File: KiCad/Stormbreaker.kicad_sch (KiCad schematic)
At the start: 46 parts, among them J1 Micro_SD_Card_Det2, J2 USB_C_Receptacle_USB2.0_14P, J3 Conn_01x03, J4 FAN, J5 Conn_01x02, Q1 PMOS, Q2 NMOS, SW1 SW_Push, U1 BQ25895RTW, U3 ATtiny1616-M

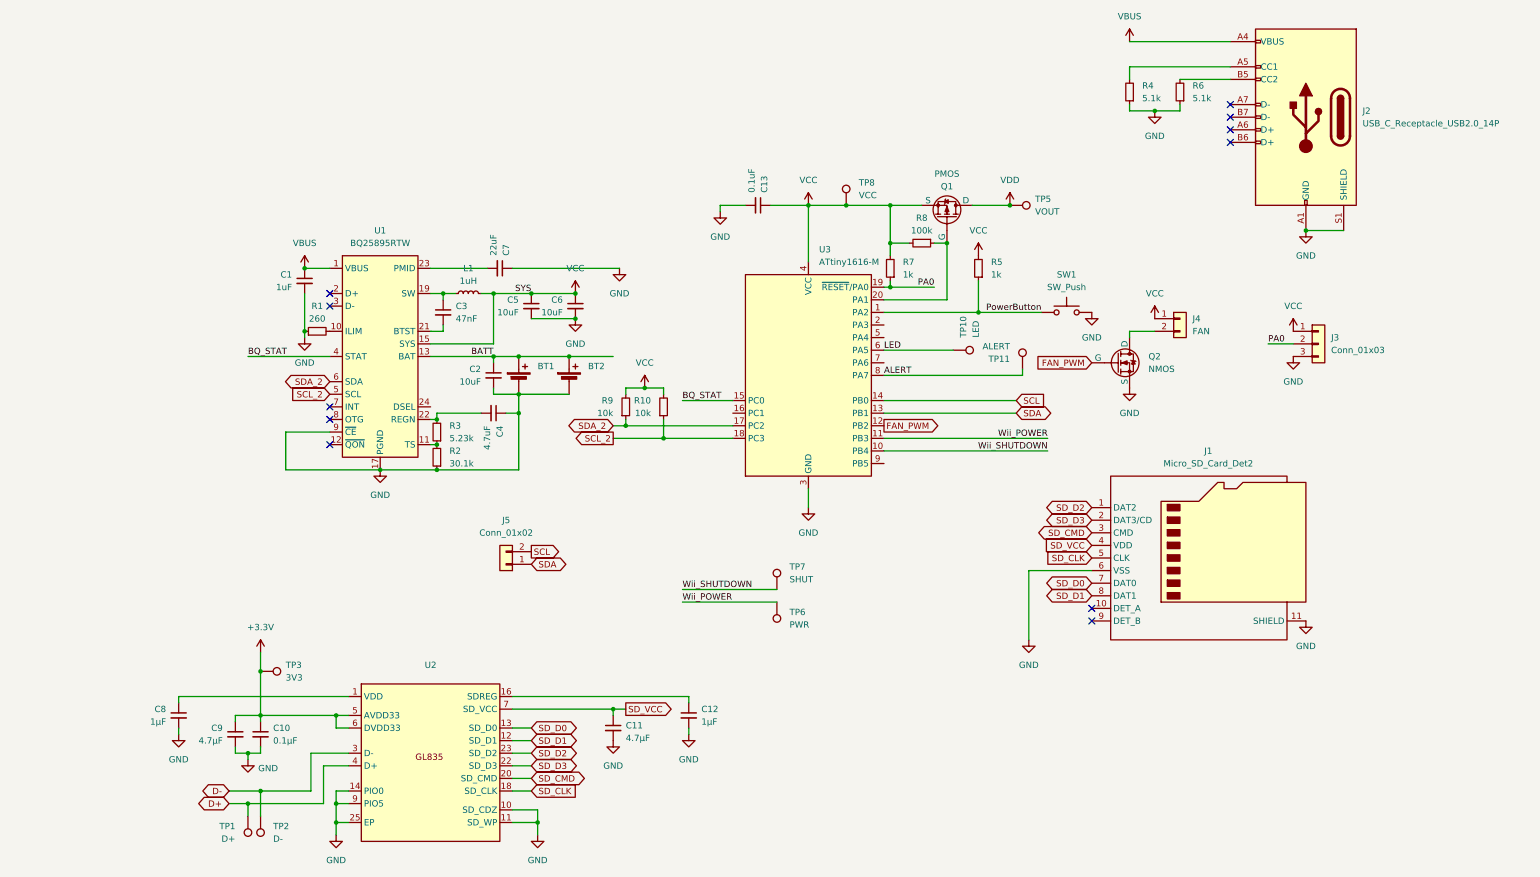
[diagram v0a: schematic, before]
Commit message: Add USB-C PD circuitry
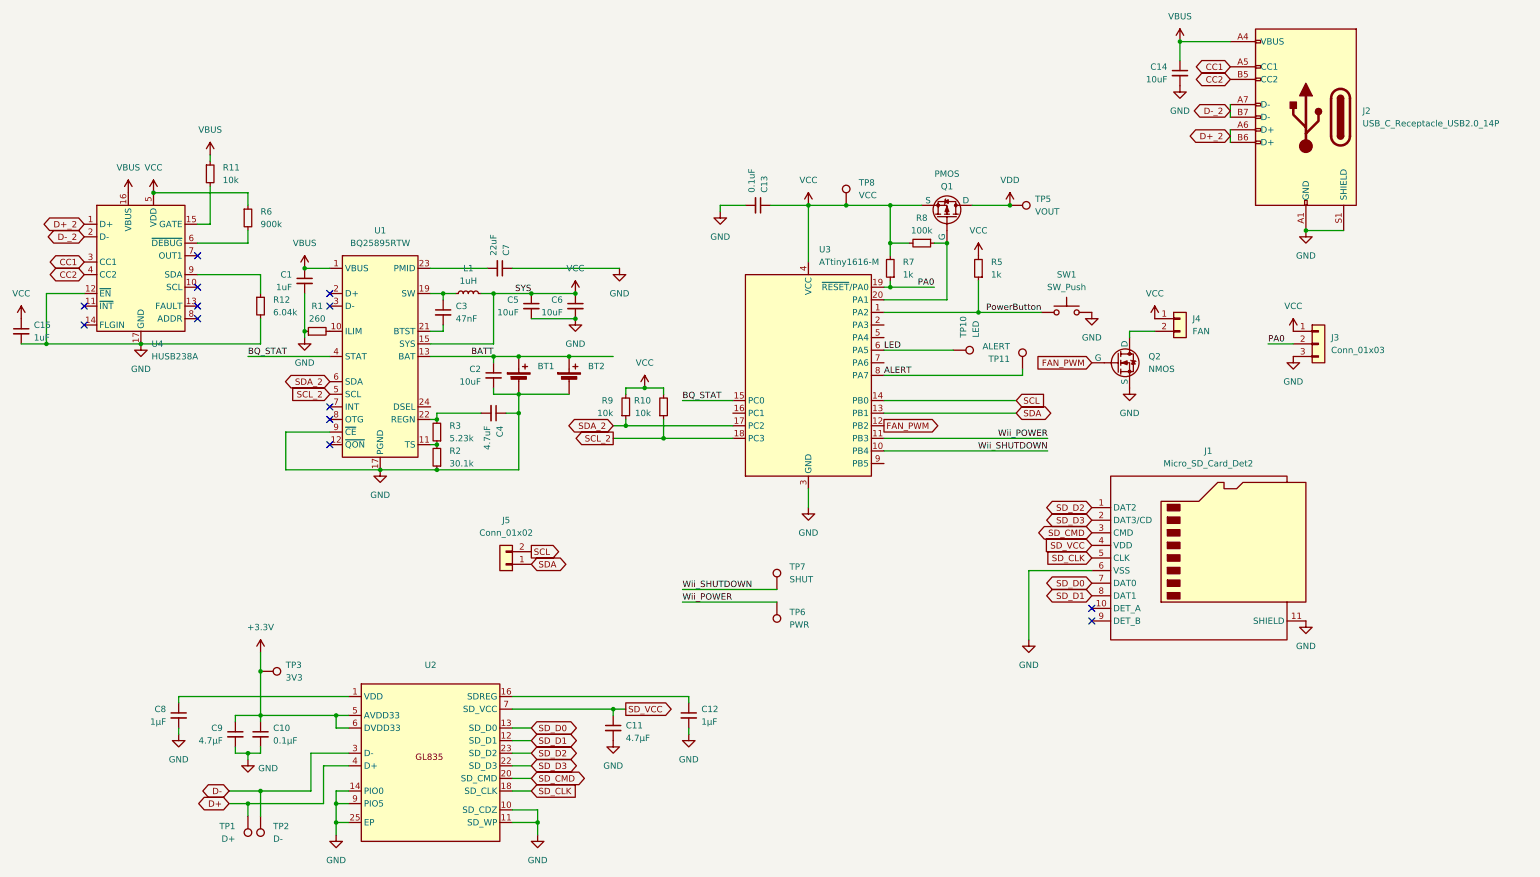
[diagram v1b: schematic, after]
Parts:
- removed R4: 5.1k, Resistor_SMD:R_0603_1608Metric, symbol Device:R_Small
- added C14: 10uF, Capacitor_SMD:C_0603_1608Metric, symbol Device:C_Small
- added C15: 1uF, Capacitor_SMD:C_0402_1005Metric, symbol Device:C_Small
- added R11: 10k, Resistor_SMD:R_0402_1005Metric, symbol Device:R_Small
- added R12: 6.04k, Resistor_SMD:R_0402_1005Metric, symbol Device:R_Small
- added U4: HUSB238A, Package_DFN_QFN:QFN-16-1EP_3x3mm_P0.5mm_EP1.7x1.7mm_ThermalVias, symbol Stormbreaker:HUSB238A
- R6: value 5.1k -> 900k; footprint Resistor_SMD:R_0603_1608Metric -> Resistor_SMD:R_0402_1005Metric
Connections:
- net GND: now also C14.2, C15.2, R12.2, U4.12 (~{EN}), U4.17 (GND); no longer R6.1
- net VBUS: now also C14.1, R11.1, U4.16 (VBUS)
- net VCC: now also R6.1, C15.1, U4.5 (VDD)
- net at R6.2: now also U4.6 (~{DEBUG}); no longer J2.B5 (CC2)
- net CC1: now reaches J2.A5 (CC1)
- net CC1: now also U4.3 (CC1)
- net D+_2: now reaches J2.A6 (D+)
- net D+_2: now also J2.B6 (D+), U4.1 (D+)
- net D-_2: now reaches J2.A7 (D-)
- net D-_2: now also J2.B7 (D-), U4.2 (D-)
- new net: R11.2, U4.15 (GATE)
- new net: R12.1, U4.9 (SDA)
- new net CC2: J2.B5 (CC2), U4.4 (CC2)
- no-connect marks 11 -> 13

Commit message: Adjustments to PD chip, WIP
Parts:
- C15: value 1uF -> 1μF
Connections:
- net VBUS: now also R6.1
- net VCC: no longer C15.1, R6.1, U4.5 (VDD)
- removed net D+_2: J2.A6 (D+), J2.B6 (D+), U4.1 (D+)
- removed net D-_2: J2.A7 (D-), J2.B7 (D-), U4.2 (D-)
- new net: C15.1, U4.5 (VDD)
- no-connect marks 13 -> 19

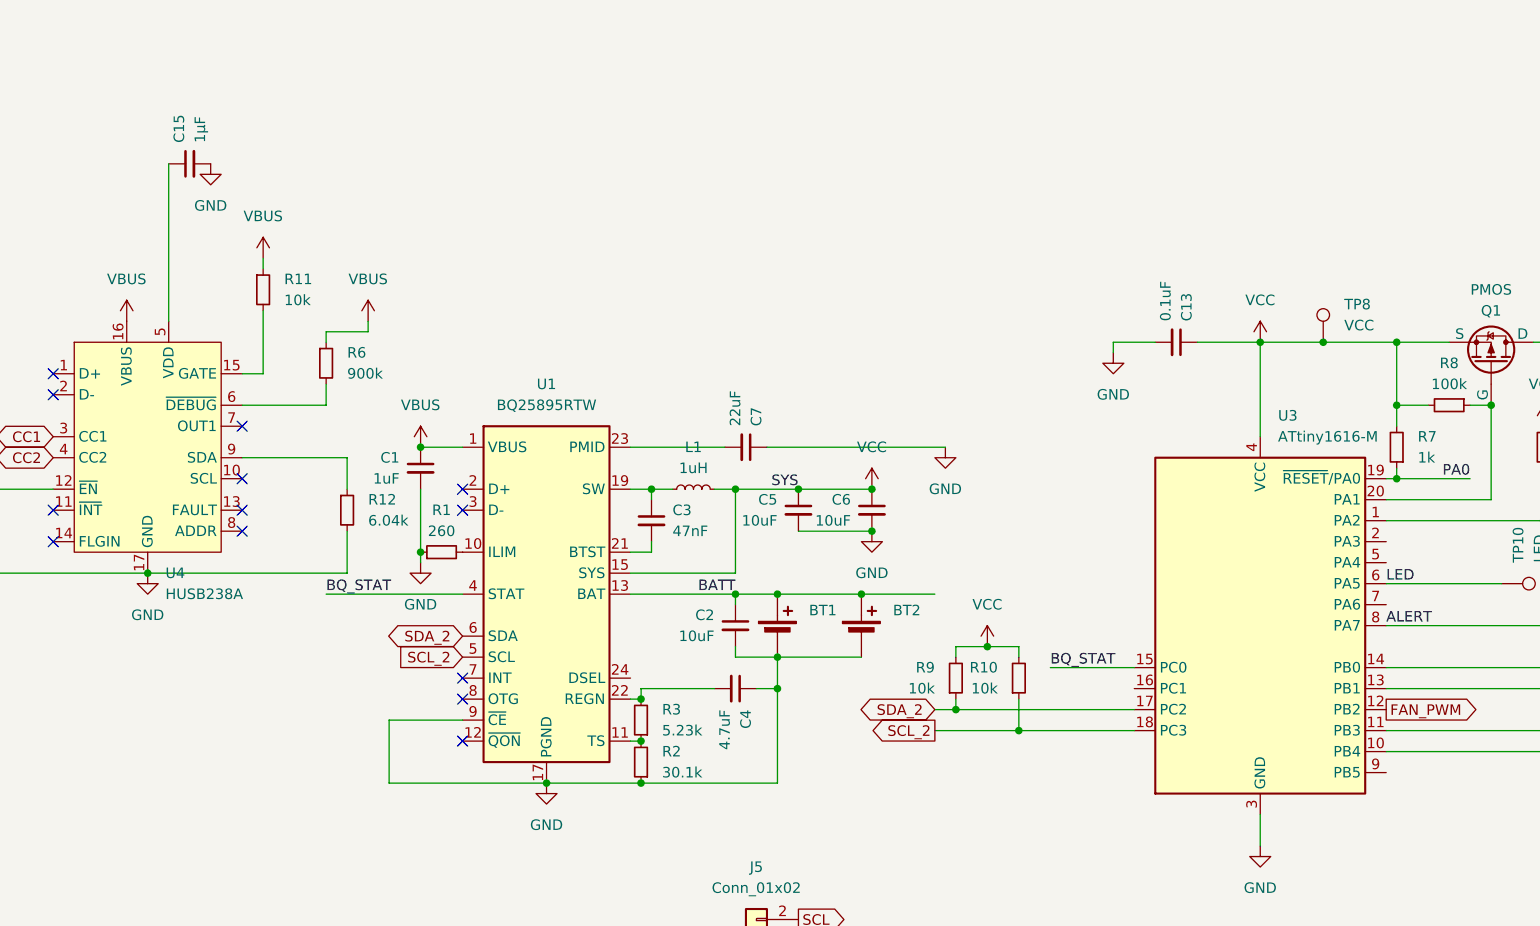
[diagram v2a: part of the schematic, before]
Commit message: Teardropped pads, slight footprint adjustments
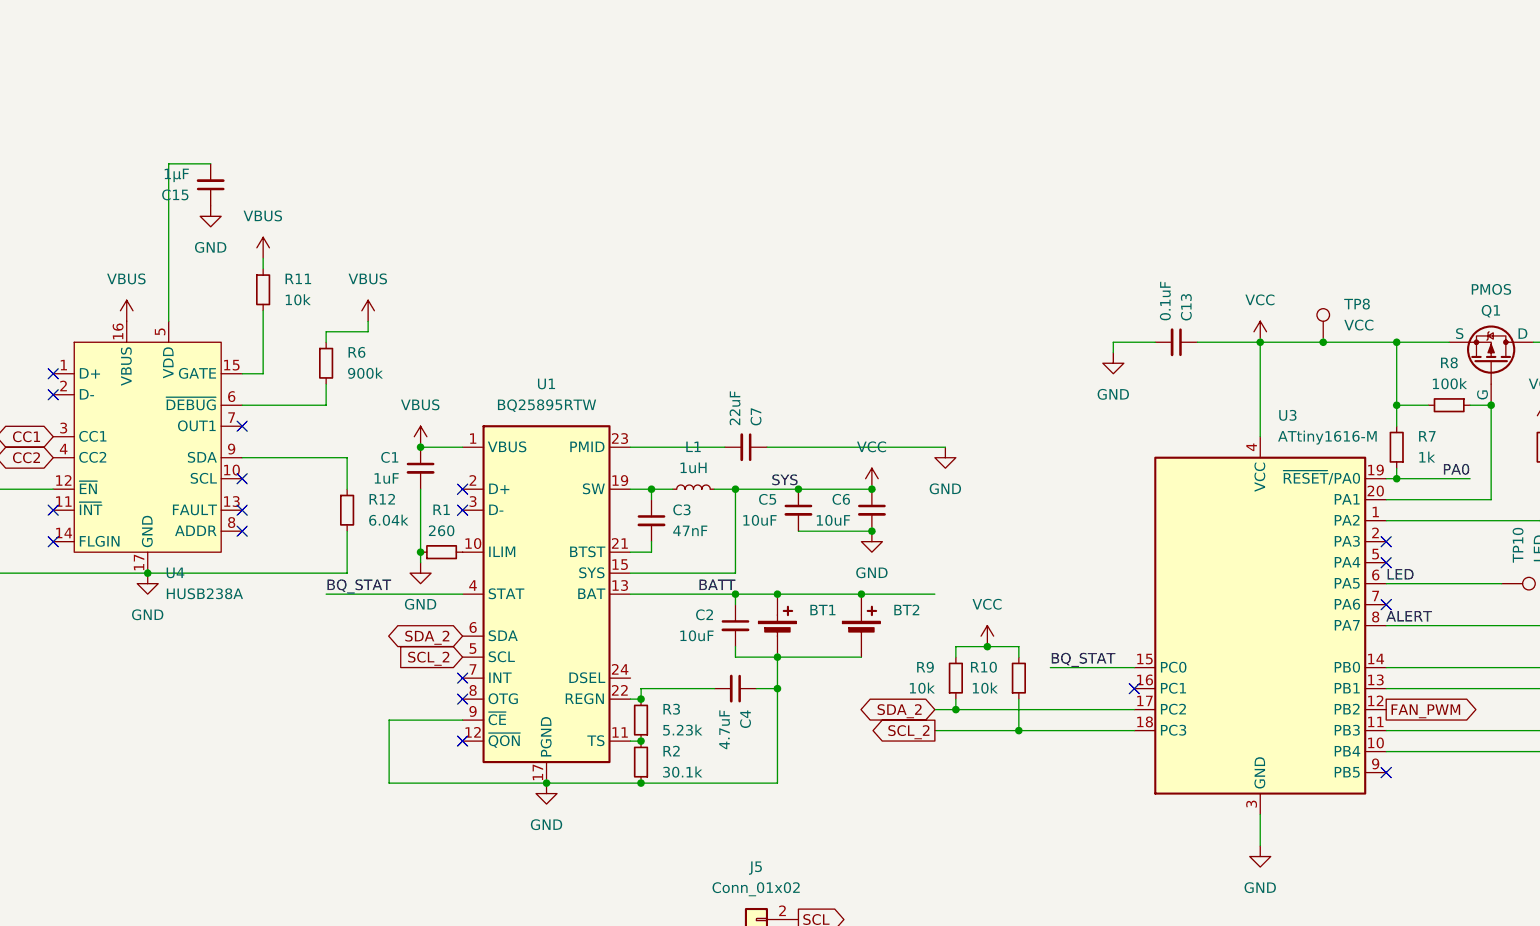
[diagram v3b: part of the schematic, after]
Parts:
- C15: footprint Capacitor_SMD:C_0402_1005Metric -> Capacitor_SMD:C_0603_1608Metric
- TP1, TP2, TP6, TP7: footprint TestPoint:TestPoint_Pad_D1.0mm -> Stormbreaker:TestPoint_Pad_D1.0mm_Small
- TP10, TP11: footprint TestPoint:TestPoint_Pad_D1.0mm -> Stormbreaker:TestPoint_Pad_D0.75mm_Small
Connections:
- net GND: now also C15.1; no longer C15.2
- net at U4.5 (VDD): now also C15.2; no longer C15.1
- no-connect marks 19 -> 24
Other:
- moved on the sheet: C15
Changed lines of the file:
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@@
 	)
 	(no_connect
+		(at 187.96 77.47)
+	)
+	(no_connect
 		(at 257.81 33.02)
 	)
 	(no_connect
+		(at 157.48 95.25)
+	)
+	(no_connect
 		(at 76.2 73.66)
 	)
@@
 	)
 	(no_connect
+		(at 187.96 105.41)
+	)
+	(no_connect
 		(at 229.87 134.62)
 	)
@@
 	)
 	(no_connect
+		(at 187.96 85.09)
+	)
+	(no_connect
+		(at 187.96 80.01)
+	)
+	(no_connect
 		(at 49.53 63.5)
 	)
@@
 	(wire
 		(pts
+			(xy 40.64 31.75) (xy 45.72 31.75)
+		)
+		(stroke
+			(width 0)
+			(type default)
+		)
+	)
+	(wire
+		(pts
 			(xy 147.32 92.71) (xy 157.48 92.71)
 		)
@@
 			)
 		)
-		(property "Footprint" "TestPoint:TestPoint_Pad_D1.0mm"
+		(property "Footprint" "Stormbreaker:TestPoint_Pad_D0.75mm_Small"
 			(at 201.93 87.63 0)
 			(effects
@@
 		(lib_name "GND_1")
 		(lib_id "power:GND")
-		(at 45.72 31.75 0)
+		(at 45.72 36.83 0)
 		(unit 1)
 		(exclude_from_sim no)
@@
 		(fields_autoplaced yes)
 		(property "Reference" "#PWR034"
-			(at 45.72 38.1 0)
+			(at 45.72 43.18 0)
 			(effects
 				(font
@@
 		)
 		(property "Value" "GND"
-			(at 45.72 36.83 0)
+			(at 45.72 41.91 0)
 			(effects
 				(font
@@
 		)
 		(property "Footprint" ""
-			(at 45.72 31.75 0)
+			(at 45.72 36.83 0)
 			(effects
 				(font
@@
 		)
 		(property "Datasheet" ""
-			(at 45.72 31.75 0)
+			(at 45.72 36.83 0)
 			(effects
 				(font
@@
 		)
 		(property "Description" "Power symbol creates a global label with name \"GND\" , ground"
-			(at 45.72 31.75 0)
+			(at 45.72 36.83 0)
 			(effects
 				(font
@@
 			)
 		)
-		(property "Footprint" "TestPoint:TestPoint_Pad_D1.0mm"
+		(property "Footprint" "Stormbreaker:TestPoint_Pad_D1.0mm_Small"
 			(at 171.45 130.81 0)
 			(effects
@@
 			)
 		)
-		(property "Footprint" "TestPoint:TestPoint_Pad_D1.0mm"
+		(property "Footprint" "Stormbreaker:TestPoint_Pad_D1.0mm_Small"
 			(at 161.29 133.35 0)
 			(effects
@@
 			)
 		)
-		(property "Footprint" "TestPoint:TestPoint_Pad_D1.0mm"
+		(property "Footprint" "Stormbreaker:TestPoint_Pad_D1.0mm_Small"
 			(at 57.15 176.53 0)
 			(effects
@@
 	(symbol
 		(lib_id "Device:C_Small")
-		(at 43.18 31.75 90)
+		(at 45.72 34.29 180)
 		(unit 1)
 		(exclude_from_sim no)
@@
 		(dnp no)
 		(property "Reference" "C15"
-			(at 41.9162 29.21 0)
+			(at 43.18 35.5538 0)
 			(effects
 				(font
@@
 		)
 		(property "Value" "1μF"
-			(at 44.4562 29.21 0)
+			(at 43.18 33.0138 0)
 			(effects
 				(font
@@
 			)
 		)
-		(property "Footprint" "Capacitor_SMD:C_0402_1005Metric"
-			(at 43.18 31.75 0)
+		(property "Footprint" "Capacitor_SMD:C_0603_1608Metric"
+			(at 45.72 34.29 0)
 			(effects
 				(font
@@
 		)
 		(property "Datasheet" "~"
-			(at 43.18 31.75 0)
+			(at 45.72 34.29 0)
 			(effects
 				(font
@@
 		)
 		(property "Description" "Unpolarized capacitor, small symbol"
-			(at 43.18 31.75 0)
+			(at 45.72 34.29 0)
 			(effects
 				(font
@@
 			)
 		)
-		(property "Footprint" "TestPoint:TestPoint_Pad_D1.0mm"
+		(property "Footprint" "Stormbreaker:TestPoint_Pad_D0.75mm_Small"
 			(at 220.98 86.36 0)
 			(effects
@@
 			)
 		)
-		(property "Footprint" "TestPoint:TestPoint_Pad_D1.0mm"
+		(property "Footprint" "Stormbreaker:TestPoint_Pad_D1.0mm_Small"
 			(at 64.77 176.53 0)
 			(effects

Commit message: Minor repositioning
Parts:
- J3: value Conn_01x03 -> PROG
- J5: value Conn_01x02 -> I2C
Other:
- moved on the sheet: R12
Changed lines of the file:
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@@
 	(wire
 		(pts
-			(xy 62.23 71.12) (xy 62.23 67.31)
+			(xy 54.61 71.12) (xy 54.61 67.31)
 		)
 		(stroke
@@
 	(wire
 		(pts
-			(xy 19.05 81.28) (xy 38.1 81.28)
+			(xy 24.13 81.28) (xy 38.1 81.28)
 		)
 		(stroke
@@
 	(wire
 		(pts
-			(xy 62.23 76.2) (xy 62.23 81.28)
+			(xy 54.61 76.2) (xy 54.61 81.28)
 		)
 		(stroke
@@
 	(wire
 		(pts
-			(xy 19.05 71.12) (xy 19.05 81.28)
+			(xy 24.13 71.12) (xy 24.13 81.28)
 		)
 		(stroke
@@
 	(wire
 		(pts
-			(xy 38.1 81.28) (xy 62.23 81.28)
+			(xy 38.1 81.28) (xy 54.61 81.28)
 		)
 		(stroke
@@
 	(wire
 		(pts
-			(xy 26.67 71.12) (xy 19.05 71.12)
+			(xy 26.67 71.12) (xy 24.13 71.12)
 		)
 		(stroke
@@
 	(wire
 		(pts
-			(xy 62.23 67.31) (xy 49.53 67.31)
+			(xy 54.61 67.31) (xy 49.53 67.31)
 		)
 		(stroke
@@
 			)
 		)
-		(property "Value" "Conn_01x03"
+		(property "Value" "PROG"
 			(at 278.13 82.5499 0)
 			(effects
@@
 	(symbol
 		(lib_id "Device:R_Small")
-		(at 62.23 73.66 0)
+		(at 54.61 73.66 0)
 		(unit 1)
 		(exclude_from_sim no)
@@
 		(fields_autoplaced yes)
 		(property "Reference" "R12"
-			(at 64.77 72.3899 0)
+			(at 57.15 72.3899 0)
 			(effects
 				(font
@@
 		)
 		(property "Value" "6.04k"
-			(at 64.77 74.9299 0)
+			(at 57.15 74.9299 0)
 			(effects
 				(font
@@
 		)
 		(property "Footprint" "Resistor_SMD:R_0402_1005Metric"
-			(at 62.23 73.66 0)
+			(at 54.61 73.66 0)
 			(effects
 				(font
@@
 		)
 		(property "Datasheet" "~"
-			(at 62.23 73.66 0)
+			(at 54.61 73.66 0)
 			(effects
 				(font
@@
 		)
 		(property "Description" "Resistor, small symbol"
-			(at 62.23 73.66 0)
+			(at 54.61 73.66 0)
 			(effects
 				(font
@@
 			)
 		)
-		(property "Value" "Conn_01x02"
+		(property "Value" "I2C"
 			(at 111.76 119.38 0)
 			(effects

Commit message: Replace 0603 resistors with 0402s, generate BOM
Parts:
- R10, R7, R8, R9: footprint Resistor_SMD:R_0603_1608Metric -> Resistor_SMD:R_0402_1005Metric
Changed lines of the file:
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@@
 			)
 		)
-		(property "Footprint" "Resistor_SMD:R_0603_1608Metric"
+		(property "Footprint" "Resistor_SMD:R_0402_1005Metric"
 			(at 189.23 66.04 0)
 			(effects
@@
 			)
 		)
-		(property "Footprint" "Resistor_SMD:R_0603_1608Metric"
+		(property "Footprint" "Resistor_SMD:R_0402_1005Metric"
 			(at 135.89 93.98 0)
 			(effects
@@
 			)
 		)
-		(property "Footprint" "Resistor_SMD:R_0603_1608Metric"
+		(property "Footprint" "Resistor_SMD:R_0402_1005Metric"
 			(at 195.58 60.96 0)
 			(effects
@@
 			)
 		)
-		(property "Footprint" "Resistor_SMD:R_0603_1608Metric"
+		(property "Footprint" "Resistor_SMD:R_0402_1005Metric"
 			(at 143.51 93.98 0)
 			(effects

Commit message: Misc improvements
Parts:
- C1: value 1uF -> 10uF
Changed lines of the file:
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@@
 			)
 		)
-		(property "Value" "1uF"
+		(property "Value" "10uF"
 			(at 68.58 69.8562 0)
 			(effects
